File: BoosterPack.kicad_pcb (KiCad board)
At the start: 2 copper layers, 88.9 x 107.9 mm, 65 parts, among them IC1 LTC4372IMS8#TRPBF, IC2 L4940D2T12-TR, IC3 MAX738ACWE+, IC4 PJ-002A, IC5 DRV103U_2K5, J1 691137710002, J2 PRT-16763, J3 691137710002, J4 53048-0810, Q1 BSC026NE2LS5ATMA1

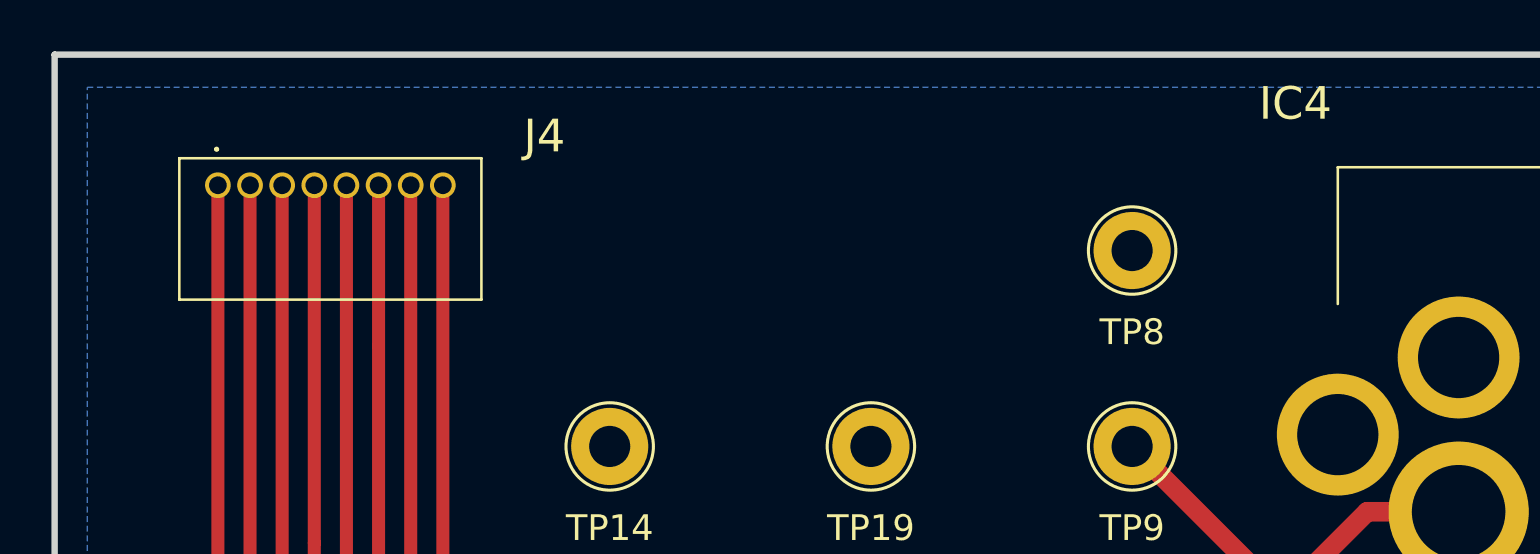
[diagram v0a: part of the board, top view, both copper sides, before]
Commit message: Updated silkscreen
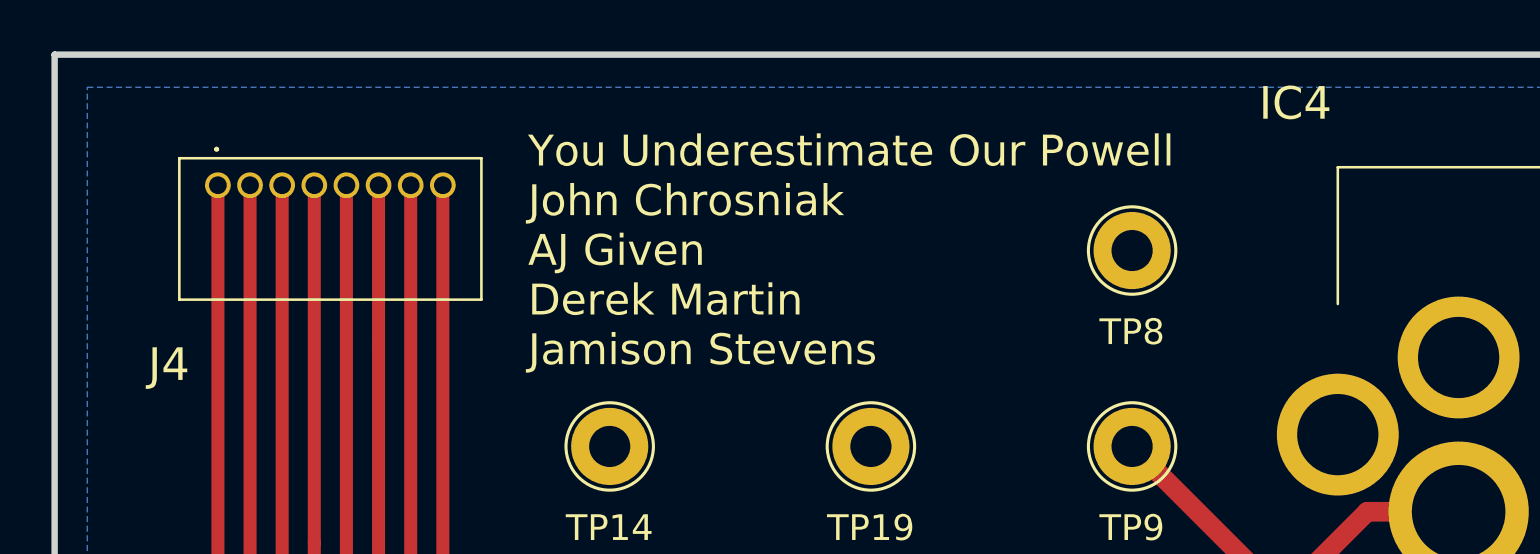
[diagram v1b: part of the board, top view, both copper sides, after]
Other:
- board text added: "You Underestimate Our Powell John Chrosniak AJ Given Derek Martin Jamison Stevens"
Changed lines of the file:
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@@
   (general
     (thickness 1.6)
-    (drawings 3)
+    (drawings 4)
     (tracks 287)
     (zones 0)
@@
     (visible_elements 7FFFFFFF)
     (pcbplotparams
-      (layerselection 0x010e0_ffffffff)
+      (layerselection 0x010f0_ffffffff)
       (usegerberextensions false)
       (usegerberattributes true)
       (usegerberadvancedattributes true)
       (creategerberjobfile true)
-      (excludeedgelayer false)
+      (excludeedgelayer true)
       (linewidth 0.100000)
       (plotframeref false)
@@
       (psa4output false)
       (plotreference true)
-      (plotvalue true)
+      (plotvalue false)
       (plotinvisibletext false)
       (padsonsilk false)
@@
       (drillshape 0)
       (scaleselection 1)
-      (outputdirectory "../"))
+      (outputdirectory "../Gerbers/"))
   )
   (net 0 "")
@@
     (descr 53048-0810-1)
     (tags Connector)
-    (fp_text reference J4 (at -12.7 1.905) (layer F.SilkS)
+    (fp_text reference J4 (at 1.905 -6.985) (layer F.SilkS)
       (effects (font (size 1.27 1.27) (thickness 0.254)))
     )
@@
     )
   )
+  (gr_text "You Underestimate Our Powell\nJohn Chrosniak\nAJ Given\nDerek Martin\nJamison Stevens" (at 113.665 50.8) (layer F.SilkS)
+    (effects (font (size 1.2 1.2) (thickness 0.3)) (justify left))
+  )
   (dimension 88.9 (width 0.15) (layer Dwgs.User)
